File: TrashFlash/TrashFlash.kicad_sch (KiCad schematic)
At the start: 2 parts, among them J101 15130322601000, J102 15230322601000

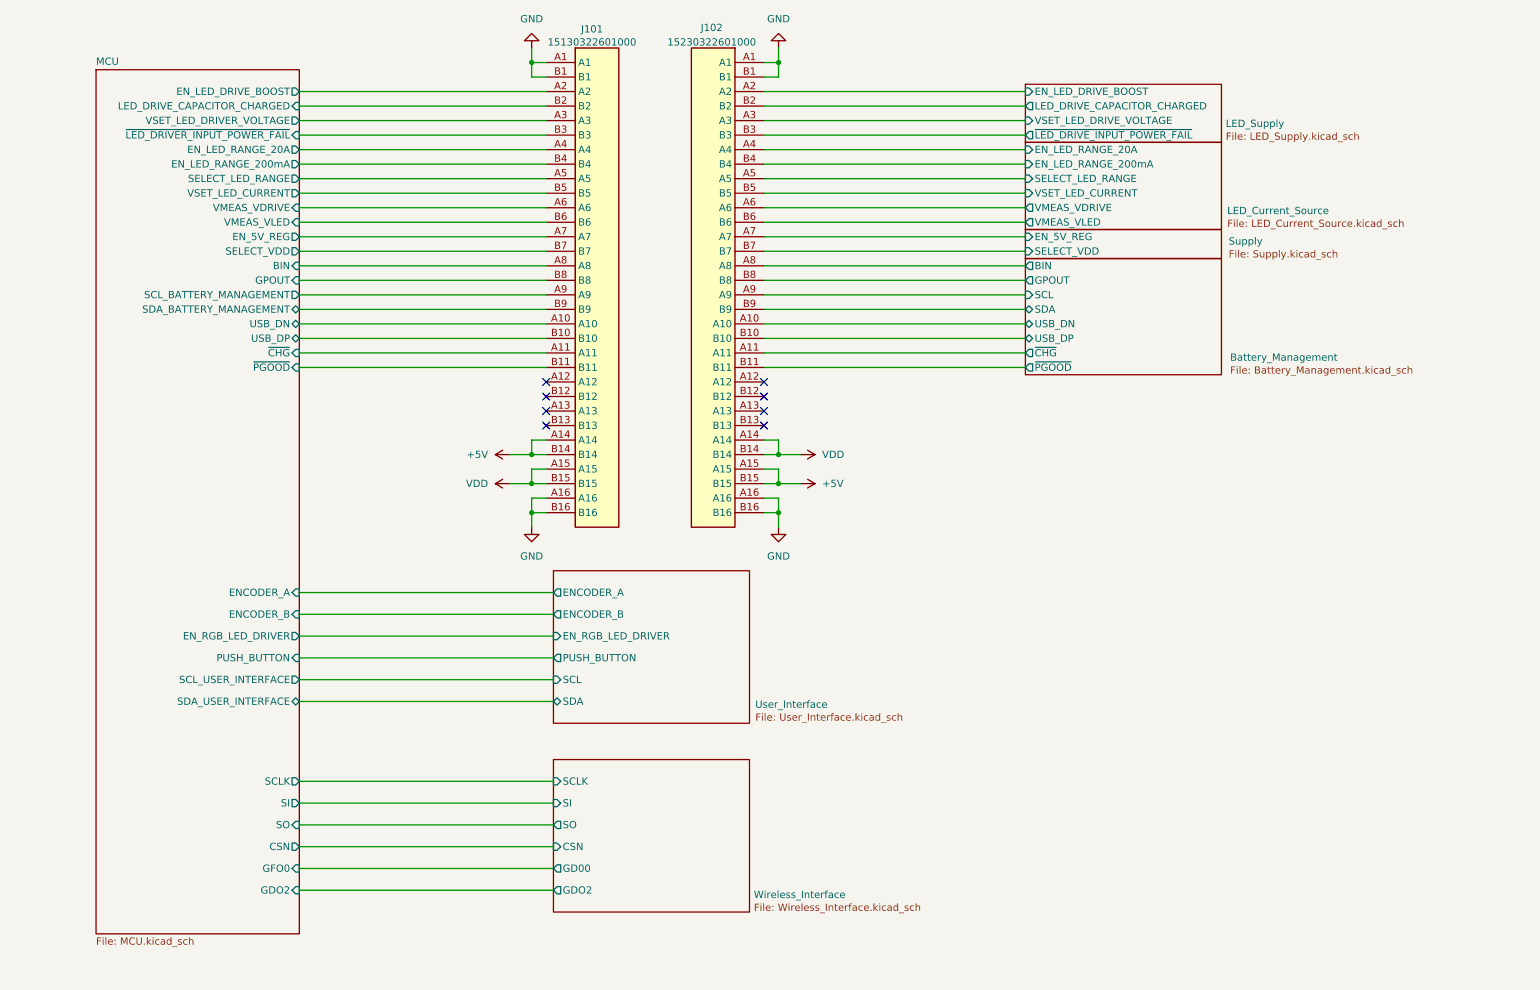
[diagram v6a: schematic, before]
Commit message: Moved USB and added JTAG connector
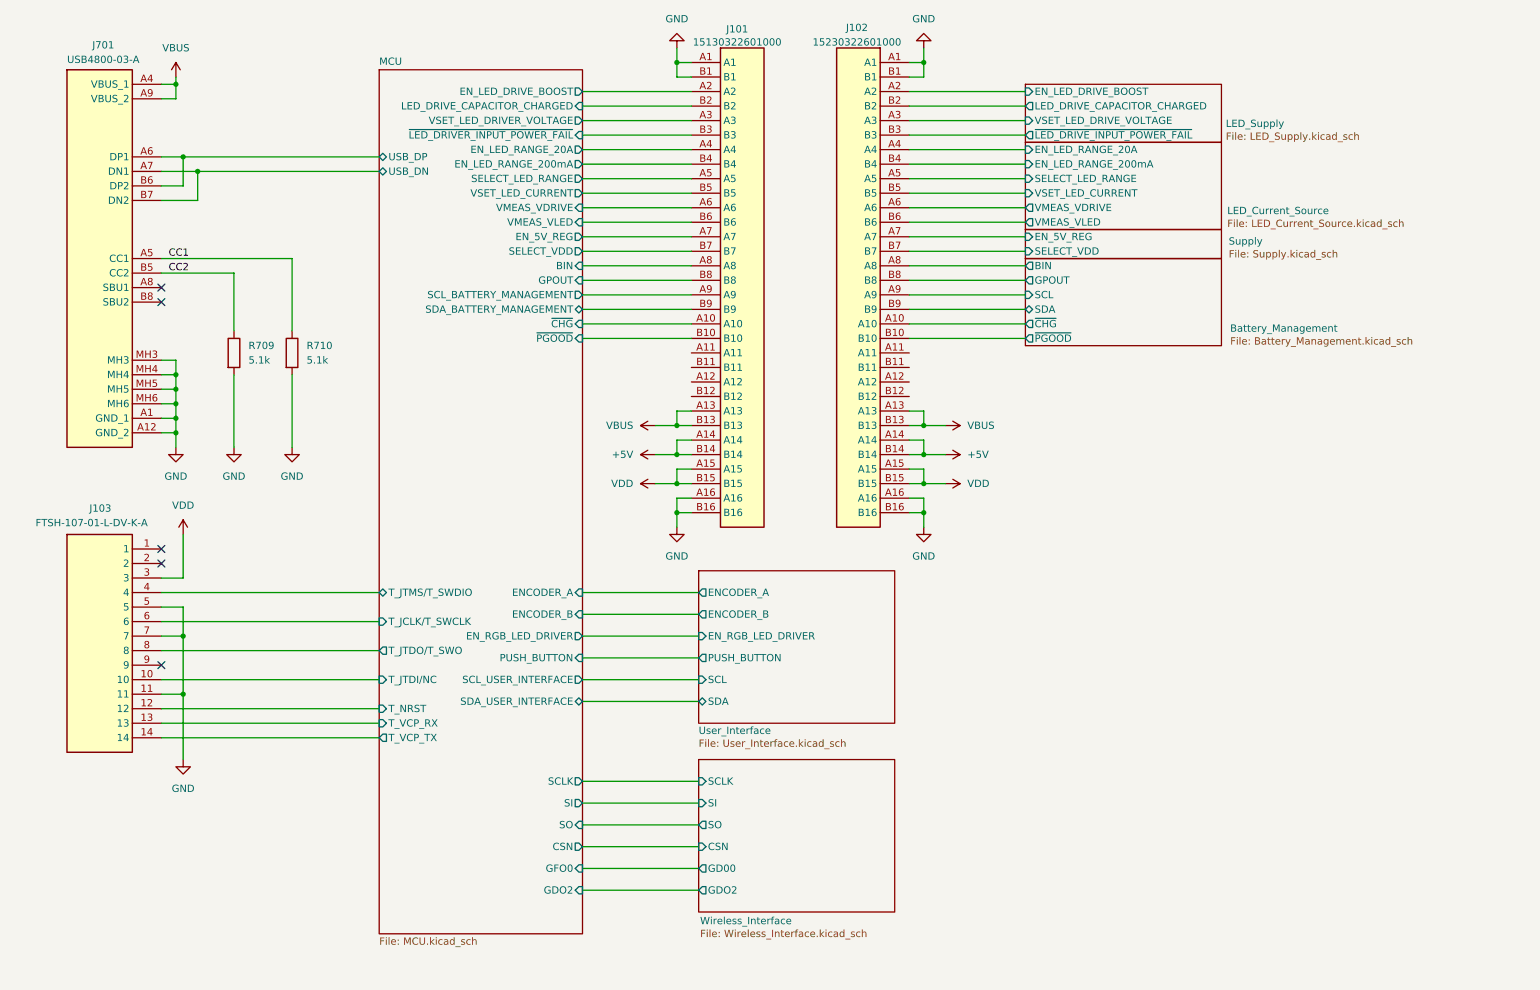
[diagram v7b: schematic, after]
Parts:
- added J103: FTSH-107-01-L-DV-K-A, FTSH-107-XX-YYY-DV-K-A, symbol TrashFlash:FTSH-107-01-L-DV-K-A
- added J701: USB4800-03-A, USB480003A, symbol TrashFlash:USB4800-03-A
- added R709, R710: 5.1k, Resistor_SMD:R_0402_1005Metric, symbol Device:R
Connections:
- net Battery_Management/USB_DN is gone; now on net Battery_Management/~{CHG}: J102.A10
- net Battery_Management/USB_DP is gone; now on net Battery_Management/~{PGOOD}: J102.B10
- net +5V: now also J102.A14, J102.B14; no longer J102.A15, J102.B15
- net Battery_Management/~{CHG}: no longer J102.A11
- net Battery_Management/~{PGOOD}: no longer J102.B11
- net GND: now also J103.11, J103.5, J103.7, J701.A1 (GND_1), J701.A12 (GND_2), J701.MH3, J701.MH4, J701.MH5, J701.MH6, R709.2, R710.2
- net MCU/USB_DN: now also J701.A7 (DN1), J701.B7 (DN2); no longer J101.A10
- net MCU/USB_DP: now also J701.A6 (DP1), J701.B6 (DP2); no longer J101.B10
- net MCU/~{CHG}: now also J101.A10; no longer J101.A11
- net MCU/~{PGOOD}: now also J101.B10; no longer J101.B11
- net VDD: now also J102.A15, J102.B15, J103.3; no longer J102.A14, J102.B14
- net VBUS: now reaches J102.A13
- net VBUS: now also J101.A13, J101.B13, J102.B13, J701.A4 (VBUS_1), J701.A9 (VBUS_2)
- new net CC1: J701.A5 (CC1), R710.1
- new net CC2: J701.B5 (CC2), R709.1
- new net MCU/T_JCLK/T_SWCLK: J103.6
- new net MCU/T_JTDI/NC: J103.10
- new net MCU/T_JTDO/T_SWO: J103.8
- new net MCU/T_JTMS/T_SWDIO: J103.4
- new net MCU/T_NRST: J103.12
- new net MCU/T_VCP_RX: J103.13
- new net MCU/T_VCP_TX: J103.14
- no-connect marks 8 -> 5
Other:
- sheet Battery_Management ports: added none; removed USB_DN, USB_DP
- sheet MCU ports: added T_JCLK/T_SWCLK, T_JTDI/NC, T_JTDO/T_SWO, T_JTMS/T_SWDIO, T_NRST, T_VCP_RX, T_VCP_TX; removed none
- moved on the sheet: J101, J102

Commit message: Added battery and connectors, Schematic remark for BQ297xx
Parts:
- J101: footprint 15130322601000 -> TrashFlash:15130322601000
- J102: footprint 15230322601000 -> TrashFlash:15230322601000
- J103: footprint FTSH-107-XX-YYY-DV-K-A -> TrashFlash:FTSH-107-XX-YYY-DV-K-A
- J701: footprint USB480003A -> TrashFlash:USB480003A
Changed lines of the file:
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@@
 			)
 		)
-		(property "Footprint" "USB480003A"
+		(property "Footprint" "TrashFlash:USB480003A"
 			(at 29.718 99.314 0)
 			(effects
@@
 			)
 		)
-		(property "Footprint" "15230322601000"
+		(property "Footprint" "TrashFlash:15230322601000"
 			(at 168.91 106.68 0)
 			(effects
@@
 			)
 		)
-		(property "Footprint" "FTSH-107-XX-YYY-DV-K-A"
+		(property "Footprint" "TrashFlash:FTSH-107-XX-YYY-DV-K-A"
 			(at 53.34 200.33 0)
 			(effects
@@
 			)
 		)
-		(property "Footprint" "15130322601000"
+		(property "Footprint" "TrashFlash:15130322601000"
 			(at 134.62 106.68 0)
 			(effects
